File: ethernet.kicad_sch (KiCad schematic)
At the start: 67 parts, among them Q6001 DMG1012T, Q6002 DMG1012T, U1001 AM6231ASGGGAALW, U6001 HR911130A, U6002 RTL8211F-CG, X6001 ECS-2520MV-250-BN-TR

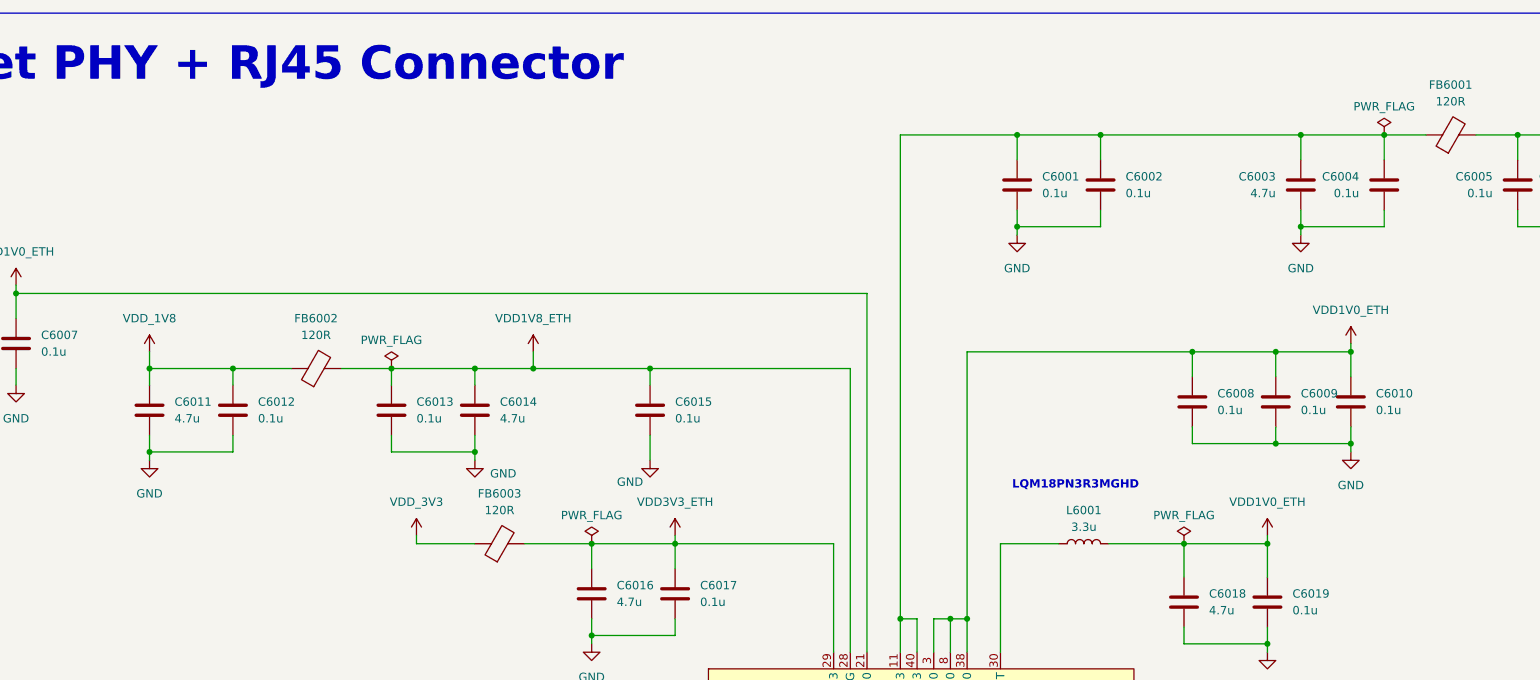
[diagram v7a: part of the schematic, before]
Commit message: More SoC fanout
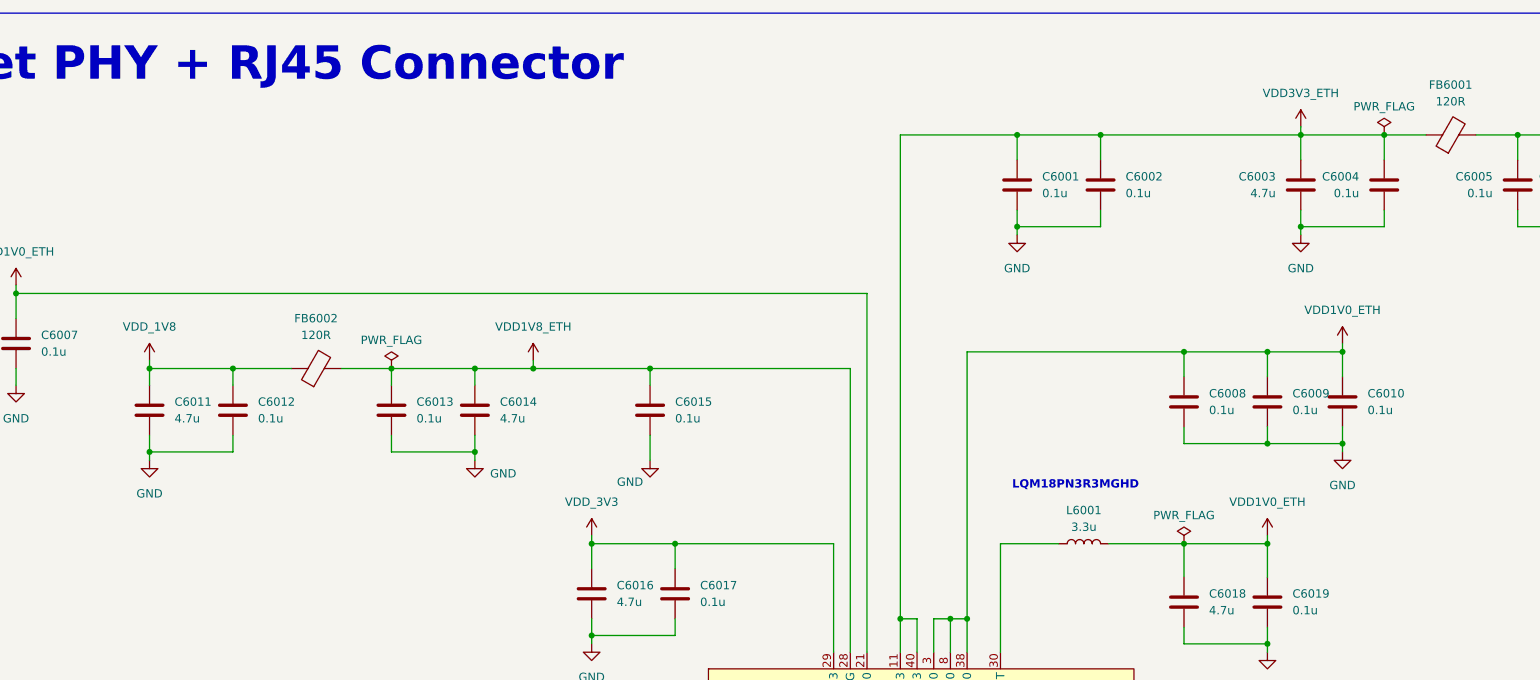
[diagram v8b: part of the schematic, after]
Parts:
- removed FB6003: 120R, Resistor_SMD:R_0402_1005Metric, symbol Device:FerriteBead
- L6001: footprint (none) -> Inductor_SMD:L_0603_1608Metric
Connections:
- net VDD3V3_ETH: now also C6001.1, C6002.1, C6003.1, C6004.1, FB6001.1, U6002.11 (AVDD33), U6002.40 (AVDD33); no longer C6016.1, C6017.1, U6002.29 (DVDD33)
- net VDD_3V3: now also C6016.1, C6017.1, U6002.29 (DVDD33)
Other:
- moved on the sheet: C6008, C6009, C6010
